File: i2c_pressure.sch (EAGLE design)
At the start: 6 parts, among them J1 Vertical Qwiic Connector, J4 Vertical Qwiic Connector, U2 SSCDANT030PASA5, U3 SSCDANT030PASA5

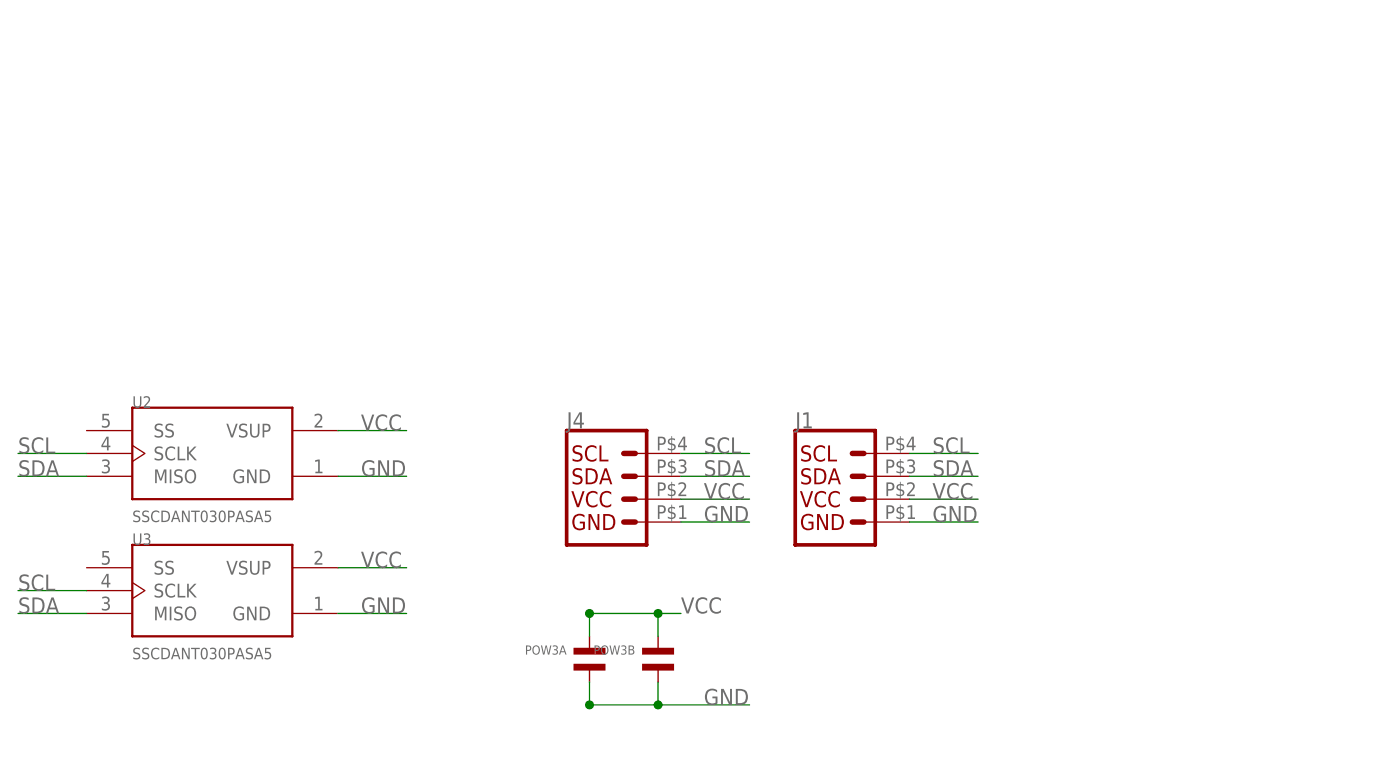
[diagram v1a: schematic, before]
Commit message: add i2c multiplexer to 00jim and pressure board
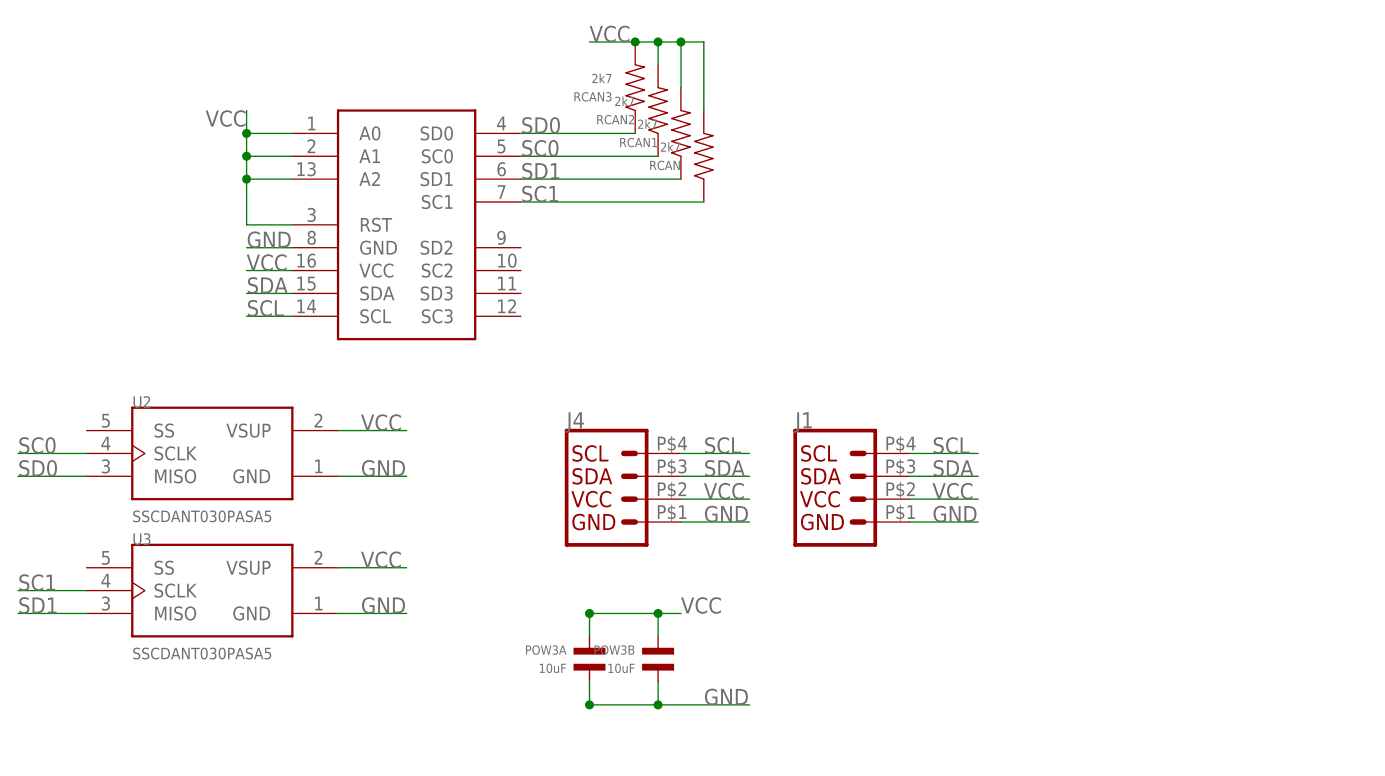
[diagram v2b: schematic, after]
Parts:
- added RCAN, RCAN1, RCAN2, RCAN3: 2k7, 00jim:RESISTOR_0603
- added U$1: TCA9546ATSSOP16, analog-devices-3:TCA9546ATSSOP16
- POW3A, POW3B: value (none) -> 10uF
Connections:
- new net SC0: RCAN2.P$1, U$1.SC0, U2.SCLK
- new net SC1: RCAN.P$1, U$1.SC1, U3.SCLK
- new net SD0: RCAN3.P$1, U$1.SD0, U2.MISO
- new net SD1: RCAN1.P$1, U$1.SD1, U3.MISO
- net GND: now also U$1.GND
- net SCL: now also U$1.SCL; no longer U2.SCLK, U3.SCLK
- net SDA: now also U$1.SDA; no longer U2.MISO, U3.MISO
- net VCC: now also RCAN.P$2, RCAN1.P$2, RCAN2.P$2, RCAN3.P$2, U$1.A0, U$1.A1, U$1.A2, U$1.RST, U$1.VCC
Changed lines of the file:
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@@
 <layers>
 <layer number="1" name="Top" color="4" fill="1" visible="no" active="no"/>
+<layer number="2" name="Route2" color="1" fill="3" visible="no" active="no"/>
+<layer number="3" name="Route3" color="4" fill="3" visible="no" active="no"/>
+<layer number="4" name="Route4" color="1" fill="4" visible="no" active="no"/>
+<layer number="5" name="Route5" color="4" fill="4" visible="no" active="no"/>
+<layer number="6" name="Route6" color="1" fill="8" visible="no" active="no"/>
+<layer number="7" name="Route7" color="4" fill="8" visible="no" active="no"/>
+<layer number="8" name="Route8" color="1" fill="2" visible="no" active="no"/>
+<layer number="9" name="Route9" color="4" fill="2" visible="no" active="no"/>
+<layer number="10" name="Route10" color="1" fill="7" visible="no" active="no"/>
+<layer number="11" name="Route11" color="4" fill="7" visible="no" active="no"/>
+<layer number="12" name="Route12" color="1" fill="5" visible="no" active="no"/>
+<layer number="13" name="Route13" color="4" fill="5" visible="no" active="no"/>
+<layer number="14" name="Route14" color="1" fill="6" visible="no" active="no"/>
+<layer number="15" name="Route15" color="4" fill="6" visible="no" active="no"/>
 <layer number="16" name="Bottom" color="9" fill="1" visible="no" active="no"/>
 <layer number="17" name="Pads" color="2" fill="1" visible="no" active="no"/>
@@
 <part name="U3" library="SSCDANT030PASA5" deviceset="SSCDANT030PASA5" device=""/>
 <part name="J4" library="00jim" deviceset="QWIIC_CONNECTOR" device="JST04_1MM_HOLE" value="Vertical Qwiic Connector"/>
-<part name="POW3B" library="MF_Passives" deviceset="CAPACITOR_NP" device="_0603"/>
-<part name="POW3A" library="MF_Passives" deviceset="CAPACITOR_NP" device="_0603"/>
+<part name="POW3B" library="MF_Passives" deviceset="CAPACITOR_NP" device="_0603" value="10uF"/>
+<part name="POW3A" library="MF_Passives" deviceset="CAPACITOR_NP" device="_0603" value="10uF"/>
 <part name="J1" library="00jim" deviceset="QWIIC_CONNECTOR" device="JST04_1MM_HOLE" value="Vertical Qwiic Connector"/>
+<part name="U$1" library="analog-devices-3" deviceset="TCA9546A" device="TSSOP16"/>
+<part name="RCAN" library="00jim" deviceset="RESISTOR" device="_0603" value="2k7"/>
+<part name="RCAN1" library="00jim" deviceset="RESISTOR" device="_0603" value="2k7"/>
+<part name="RCAN2" library="00jim" deviceset="RESISTOR" device="_0603" value="2k7"/>
+<part name="RCAN3" library="00jim" deviceset="RESISTOR" device="_0603" value="2k7"/>
 </parts>
 <sheets>
@@
 <attribute name="NAME" x="104.14" y="78.994" size="1.778" layer="95" font="vector"/>
 </instance>
+<instance part="U$1" gate="G$1" x="60.96" y="106.68" smashed="yes"/>
+<instance part="RCAN" gate="G$1" x="93.98" y="109.22" smashed="yes" rot="R180">
+<attribute name="NAME" x="91.44" y="107.696" size="1.016" layer="95" font="vector" rot="R180" align="top-left"/>
+<attribute name="VALUE" x="91.44" y="110.744" size="1.016" layer="96" font="vector" rot="R180"/>
+</instance>
+<instance part="RCAN1" gate="G$1" x="91.44" y="111.76" smashed="yes" rot="R180">
+<attribute name="NAME" x="88.9" y="110.236" size="1.016" layer="95" font="vector" rot="R180" align="top-left"/>
+<attribute name="VALUE" x="88.9" y="113.284" size="1.016" layer="96" font="vector" rot="R180"/>
+</instance>
+<instance part="RCAN2" gate="G$1" x="88.9" y="114.3" smashed="yes" rot="R180">
+<attribute name="NAME" x="86.36" y="112.776" size="1.016" layer="95" font="vector" rot="R180" align="top-left"/>
+<attribute name="VALUE" x="86.36" y="115.824" size="1.016" layer="96" font="vector" rot="R180"/>
+</instance>
+<instance part="RCAN3" gate="G$1" x="86.36" y="116.84" smashed="yes" rot="R180">
+<attribute name="NAME" x="83.82" y="115.316" size="1.016" layer="95" font="vector" rot="R180" align="top-left"/>
+<attribute name="VALUE" x="83.82" y="118.364" size="1.016" layer="96" font="vector" rot="R180"/>
+</instance>
 </instances>
 <busses>
@@
 <pinref part="J1" gate="G$1" pin="1"/>
 </segment>
+<segment>
+<pinref part="U$1" gate="G$1" pin="GND"/>
+<wire x1="48.26" y1="99.06" x2="43.18" y2="99.06" width="0.1524" layer="91"/>
+<label x="43.18" y="99.06" size="1.778" layer="95"/>
+</segment>
 </net>
 <net name="SDA" class="0">
-<segment>
-<pinref part="U2" gate="G$1" pin="MISO"/>
-<wire x1="25.4" y1="73.66" x2="17.78" y2="73.66" width="0.1524" layer="91"/>
-<label x="17.78" y="73.66" size="1.778" layer="95"/>
-</segment>
-<segment>
-<pinref part="U3" gate="G$1" pin="MISO"/>
-<wire x1="25.4" y1="58.42" x2="17.78" y2="58.42" width="0.1524" layer="91"/>
-<label x="17.78" y="58.42" size="1.778" layer="95"/>
-</segment>
 <segment>
 <wire x1="91.44" y1="73.66" x2="99.06" y2="73.66" width="0.1524" layer="91"/>
@@
 <pinref part="J1" gate="G$1" pin="3"/>
 </segment>
+<segment>
+<pinref part="U$1" gate="G$1" pin="SDA"/>
+<wire x1="48.26" y1="93.98" x2="43.18" y2="93.98" width="0.1524" layer="91"/>
+<label x="43.18" y="93.98" size="1.778" layer="95"/>
+</segment>
 </net>
 <net name="SCL" class="0">
-<segment>
-<pinref part="U2" gate="G$1" pin="SCLK"/>
-<wire x1="25.4" y1="76.2" x2="17.78" y2="76.2" width="0.1524" layer="91"/>
-<label x="17.78" y="76.2" size="1.778" layer="95"/>
-</segment>
-<segment>
-<pinref part="U3" gate="G$1" pin="SCLK"/>
-<wire x1="25.4" y1="60.96" x2="17.78" y2="60.96" width="0.1524" layer="91"/>
-<label x="17.78" y="60.96" size="1.778" layer="95"/>
-</segment>
 <segment>
 <wire x1="91.44" y1="76.2" x2="99.06" y2="76.2" width="0.1524" layer="91"/>
@@
 <label x="119.38" y="76.2" size="1.778" layer="95"/>
 <pinref part="J1" gate="G$1" pin="4"/>
+</segment>
+<segment>
+<pinref part="U$1" gate="G$1" pin="SCL"/>
+<wire x1="48.26" y1="91.44" x2="43.18" y2="91.44" width="0.1524" layer="91"/>
+<label x="43.18" y="91.44" size="1.778" layer="95"/>
 </segment>
 </net>
@@
 <pinref part="J1" gate="G$1" pin="2"/>
 </segment>
-</net>
+<segment>
+<pinref part="U$1" gate="G$1" pin="A0"/>
+<wire x1="48.26" y1="111.76" x2="43.18" y2="111.76" width="0.1524" layer="91"/>
+<pinref part="U$1" gate="G$1" pin="A1"/>
+<wire x1="48.26" y1="109.22" x2="43.18" y2="109.22" width="0.1524" layer="91"/>
+<pinref part="U$1" gate="G$1" pin="A2"/>
+<wire x1="48.26" y1="106.68" x2="43.18" y2="106.68" width="0.1524" layer="91"/>
+<wire x1="43.18" y1="106.68" x2="43.18" y2="109.22" width="0.1524" layer="91"/>
+<junction x="43.18" y="109.22"/>
+<wire x1="43.18" y1="109.22" x2="43.18" y2="111.76" width="0.1524" layer="91"/>
+<junction x="43.18" y="111.76"/>
+<wire x1="43.18" y1="111.76" x2="43.18" y2="114.3" width="0.1524" layer="91"/>
+<label x="43.18" y="114.3" size="1.778" layer="95" rot="R180"/>
+<wire x1="43.18" y1="106.68" x2="43.18" y2="101.6" width="0.1524" layer="91"/>
+<junction x="43.18" y="106.68"/>
+<pinref part="U$1" gate="G$1" pin="RST"/>
+<wire x1="43.18" y1="101.6" x2="48.26" y2="101.6" width="0.1524" layer="91"/>
+</segment>
+<segment>
+<pinref part="U$1" gate="G$1" pin="VCC"/>
+<wire x1="48.26" y1="96.52" x2="43.18" y2="96.52" width="0.1524" layer="91"/>
+<label x="43.18" y="96.52" size="1.778" layer="95"/>
+</segment>
+<segment>
+<pinref part="RCAN2" gate="G$1" pin="P$2"/>
+<wire x1="88.9" y1="119.38" x2="88.9" y2="121.92" width="0.1524" layer="91"/>
+<pinref part="RCAN3" gate="G$1" pin="P$2"/>
+<wire x1="86.36" y1="121.92" x2="88.9" y2="121.92" width="0.1524" layer="91"/>
+<pinref part="RCAN1" gate="G$1" pin="P$2"/>
+<wire x1="91.44" y1="116.84" x2="91.44" y2="121.92" width="0.1524" layer="91"/>
+<wire x1="88.9" y1="121.92" x2="91.44" y2="121.92" width="0.1524" layer="91"/>
+<junction x="88.9" y="121.92"/>
+<pinref part="RCAN" gate="G$1" pin="P$2"/>
+<wire x1="93.98" y1="114.3" x2="93.98" y2="121.92" width="0.1524" layer="91"/>
+<wire x1="91.44" y1="121.92" x2="93.98" y2="121.92" width="0.1524" layer="91"/>
+<junction x="91.44" y="121.92"/>
+<junction x="86.36" y="121.92"/>
+<wire x1="86.36" y1="121.92" x2="81.28" y2="121.92" width="0.1524" layer="91"/>
+<label x="81.28" y="121.92" size="1.778" layer="95"/>
+</segment>
+</net>
+<net name="SD0" class="0">
+<segment>
+<pinref part="U$1" gate="G$1" pin="SD0"/>
+<label x="73.66" y="111.76" size="1.778" layer="95"/>
+<pinref part="RCAN3" gate="G$1" pin="P$1"/>
+<wire x1="73.66" y1="111.76" x2="86.36" y2="111.76" width="0.1524" layer="91"/>
+</segment>
+<segment>
+<pinref part="U2" gate="G$1" pin="MISO"/>
+<wire x1="25.4" y1="73.66" x2="17.78" y2="73.66" width="0.1524" layer="91"/>
+<label x="17.78" y="73.66" size="1.778" layer="95"/>
+</segment>
+</net>
+<net name="SC0" class="0">
+<segment>
+<pinref part="U$1" gate="G$1" pin="SC0"/>
+<label x="73.66" y="109.22" size="1.778" layer="95"/>
+<pinref part="RCAN2" gate="G$1" pin="P$1"/>
+<wire x1="73.66" y1="109.22" x2="88.9" y2="109.22" width="0.1524" layer="91"/>
+</segment>
+<segment>
+<pinref part="U2" gate="G$1" pin="SCLK"/>
+<wire x1="25.4" y1="76.2" x2="17.78" y2="76.2" width="0.1524" layer="91"/>
+<label x="17.78" y="76.2" size="1.778" layer="95"/>
+</segment>
+</net>
+<net name="SD1" class="0">
+<segment>
+<pinref part="U$1" gate="G$1" pin="SD1"/>
+<label x="73.66" y="106.68" size="1.778" layer="95"/>
+<pinref part="RCAN1" gate="G$1" pin="P$1"/>
+<wire x1="73.66" y1="106.68" x2="91.44" y2="106.68" width="0.1524" layer="91"/>
+</segment>
+<segment>
+<pinref part="U3" gate="G$1" pin="MISO"/>
+<wire x1="25.4" y1="58.42" x2="17.78" y2="58.42" width="0.1524" layer="91"/>
+<label x="17.78" y="58.42" size="1.778" layer="95"/>
+</segment>
+</net>
+<net name="SC1" class="0">
+<segment>
+<pinref part="U$1" gate="G$1" pin="SC1"/>
+<label x="73.66" y="104.14" size="1.778" layer="95"/>
+<pinref part="RCAN" gate="G$1" pin="P$1"/>
+<wire x1="73.66" y1="104.14" x2="93.98" y2="104.14" width="0.1524" layer="91"/>
+</segment>
+<segment>
+<pinref part="U3" gate="G$1" pin="SCLK"/>
+<wire x1="25.4" y1="60.96" x2="17.78" y2="60.96" width="0.1524" layer="91"/>
+<label x="17.78" y="60.96" size="1.778" layer="95"/>
+</segment>
+</net>
